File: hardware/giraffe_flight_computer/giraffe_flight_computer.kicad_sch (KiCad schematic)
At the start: 6 parts, among them J16 ADC, J2 PI, J4 ADC, J5 BAT, J6 BAT, J8 PI

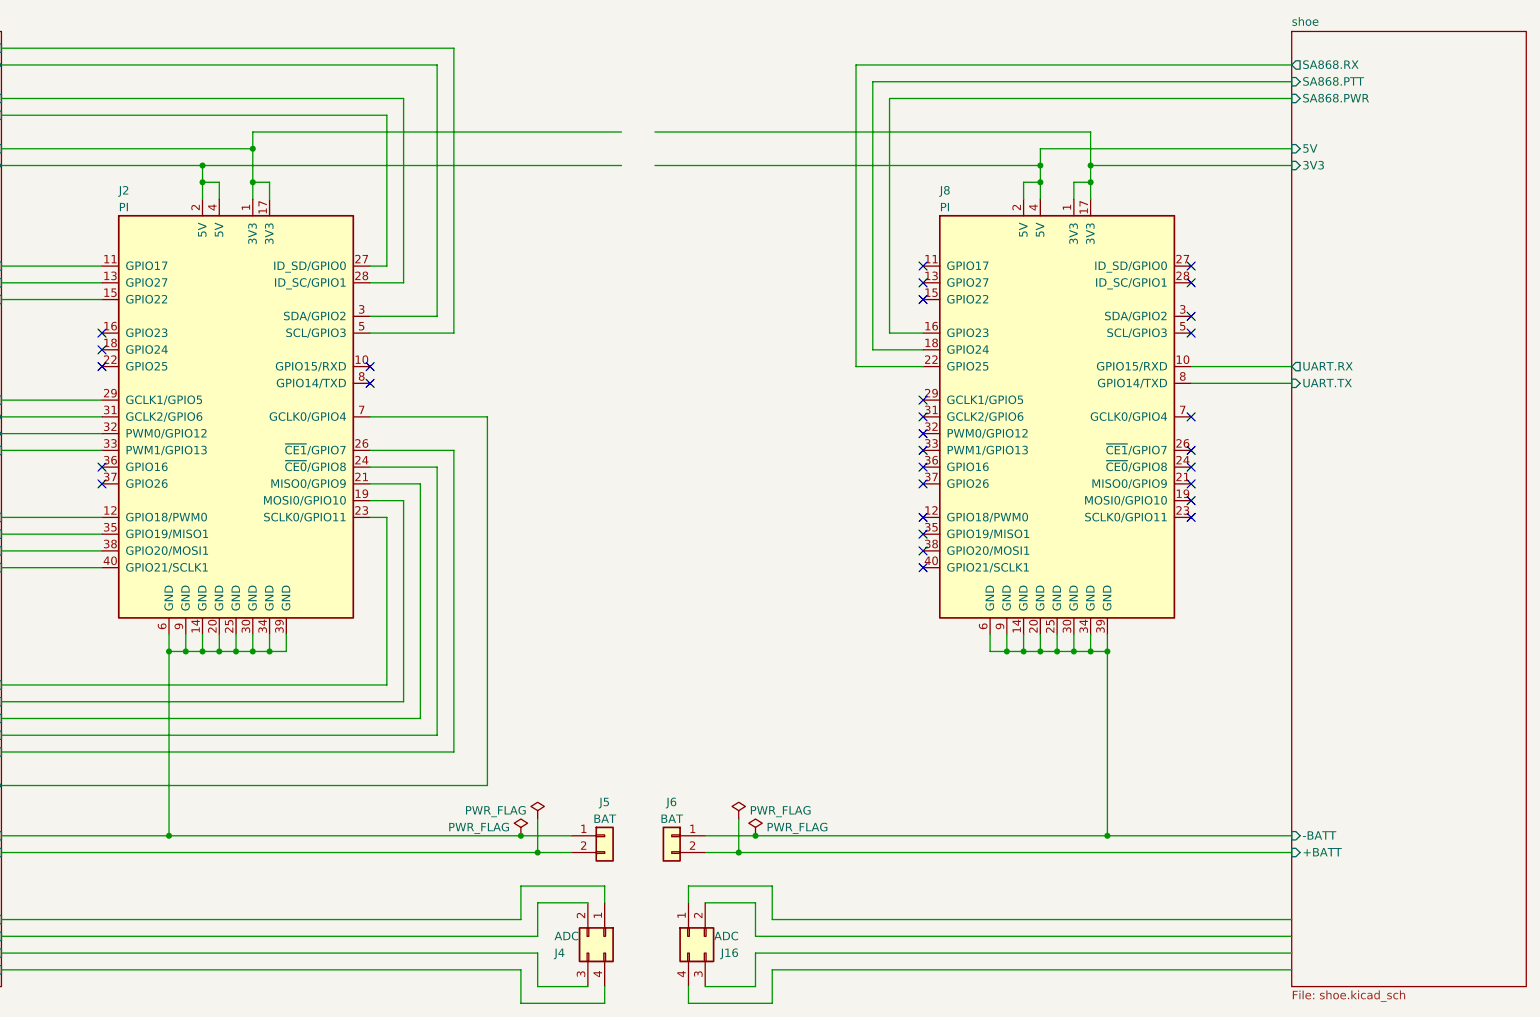
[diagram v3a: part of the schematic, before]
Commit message: More Schematic changes
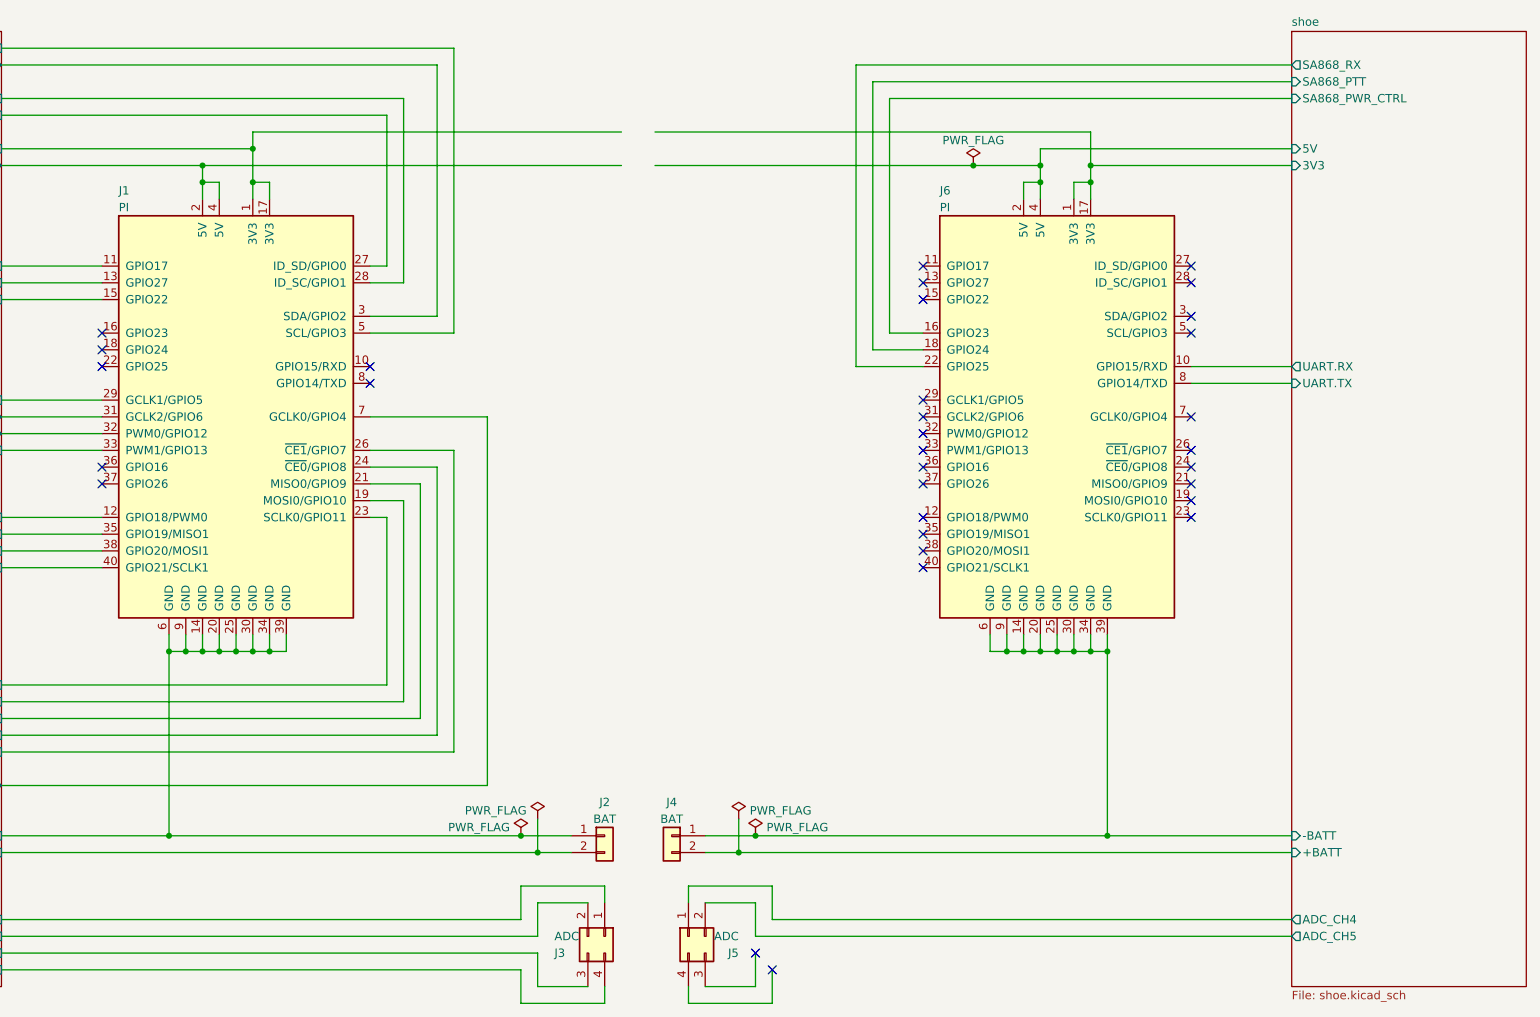
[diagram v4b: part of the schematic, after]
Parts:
- J2: renamed from J5; footprint (none) -> giraffe_flight_computer_footprints:battery_connection
- J4: renamed from J6; footprint (none) -> giraffe_flight_computer_footprints:battery_connection
- renumbered J2 to J1, J4 to J3, J16 to J5, J8 to J6
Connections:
- net shoe/ADC_CH4: now reaches J5.1 (Pin_1)
- net shoe/ADC_CH5: now reaches J5.2 (Pin_2)
- net shoe/SA868.PTT renamed shoe/SA868_PTT
- net shoe/SA868.PWR renamed shoe/SA868_PWR_CTRL
- net shoe/SA868.RX renamed shoe/SA868_RX
- no-connect marks 30 -> 32
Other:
- sheet shoe ports: added ADC_CH4, ADC_CH5, SA868_PTT, SA868_PWR_CTRL, SA868_RX; removed SA868.PTT, SA868.PWR, SA868.RX
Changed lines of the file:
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@@
   (junction (at 88.9 109.22) (diameter 0) (color 0 0 0 0)
+  )
+  (junction (at 198.12 35.56) (diameter 0) (color 0 0 0 0)
   )
   (junction (at 81.28 109.22) (diameter 0) (color 0 0 0 0)
@@
   (no_connect (at 231.14 78.74))
   (no_connect (at 231.14 58.42))
+  (no_connect (at 167.64 157.48))
   (no_connect (at 190.5 88.9))
   (no_connect (at 231.14 81.28))
@@
   (no_connect (at 231.14 53.34))
   (no_connect (at 190.5 93.98))
+  (no_connect (at 165.1 154.94))
   (no_connect (at 66.04 83.82))
   (no_connect (at 190.5 71.12))
@@
     (stroke (width 0) (type default))
   )
-  (wire (pts (xy 246.38 157.48) (xy 167.64 157.48))
-    (stroke (width 0) (type default))
-  )
   (wire (pts (xy 106.68 78.74) (xy 119.38 78.74))
     (stroke (width 0) (type default))
@@
     (stroke (width 0) (type default))
   )
-  (wire (pts (xy 246.38 154.94) (xy 165.1 154.94))
-    (stroke (width 0) (type default))
-  )
   (wire (pts (xy 162.56 139.7) (xy 246.38 139.7))
     (stroke (width 0) (type default))
@@
     (stroke (width 0) (type default))
   )
-  (wire (pts (xy 149.86 35.56) (xy 208.28 35.56))
+  (wire (pts (xy 149.86 35.56) (xy 198.12 35.56))
     (stroke (width 0) (type default))
   )
@@
   )
   (wire (pts (xy 157.48 137.16) (xy 165.1 137.16))
+    (stroke (width 0) (type default))
+  )
+  (wire (pts (xy 198.12 35.56) (xy 208.28 35.56))
     (stroke (width 0) (type default))
   )
@@
   (symbol (lib_id "giraffe_symbols:pi_zero") (at 210.82 73.66 0) (unit 1)
     (in_bom yes) (on_board yes) (dnp no)
-    (property "Reference" "J8" (at 193.04 39.37 0)
+    (property "Reference" "J6" (at 193.04 39.37 0)
       (effects (font (size 1.27 1.27)) (justify left))
     )
@@
       (project "giraffe_flight_computer"
         (path "/8b6d32d3-7736-4ef0-bfd7-9f676eec710d"
-          (reference "J8") (unit 1)
+          (reference "J6") (unit 1)
         )
       )
@@
   (symbol (lib_id "Connector_Generic:Conn_02x02_Counter_Clockwise") (at 142.24 152.4 270) (unit 1)
     (in_bom yes) (on_board yes) (dnp no)
-    (property "Reference" "J4" (at 134.62 154.94 90)
+    (property "Reference" "J3" (at 134.62 154.94 90)
       (effects (font (size 1.27 1.27)) (justify left))
     )
@@
       (project "giraffe_flight_computer"
         (path "/8b6d32d3-7736-4ef0-bfd7-9f676eec710d"
-          (reference "J4") (unit 1)
+          (reference "J3") (unit 1)
         )
       )
@@
   (symbol (lib_id "Connector_Generic:Conn_01x02") (at 152.4 137.16 0) (mirror y) (unit 1)
     (in_bom yes) (on_board yes) (dnp no)
-    (property "Reference" "J6" (at 152.4 132.08 0)
+    (property "Reference" "J4" (at 152.4 132.08 0)
       (effects (font (size 1.27 1.27)))
     )
@@
       (effects (font (size 1.27 1.27)))
     )
-    (property "Footprint" "" (at 152.4 137.16 0)
+    (property "Footprint" "giraffe_flight_computer_footprints:battery_connection" (at 152.4 137.16 0)
       (effects (font (size 1.27 1.27)) hide)
     )
@@
       (project "giraffe_flight_computer"
         (path "/8b6d32d3-7736-4ef0-bfd7-9f676eec710d"
-          (reference "J6") (unit 1)
+          (reference "J4") (unit 1)
+        )
+      )
+    )
+  )
+  (symbol (lib_id "power:PWR_FLAG") (at 198.12 35.56 0) (unit 1)
+    (in_bom yes) (on_board yes) (dnp no)
+    (property "Reference" "#FLG?" (at 198.12 33.655 0)
+      (effects (font (size 1.27 1.27)) hide)
+    )
+    (property "Value" "PWR_FLAG" (at 198.12 31.75 0)
+      (effects (font (size 1.27 1.27)))
+    )
+    (property "Footprint" "" (at 198.12 35.56 0)
+      (effects (font (size 1.27 1.27)) hide)
+    )
+    (property "Datasheet" "~" (at 198.12 35.56 0)
+      (effects (font (size 1.27 1.27)) hide)
+    )
+    (pin "1")
+    (instances
+      (project "giraffe_flight_computer"
+        (path "/8b6d32d3-7736-4ef0-bfd7-9f676eec710d/ba60804d-01a4-423f-89a4-e92a0bf73814"
+          (reference "#FLG?") (unit 1)
+        )
+        (path "/8b6d32d3-7736-4ef0-bfd7-9f676eec710d"
+          (reference "#FLG05") (unit 1)
         )
       )
@@
   (symbol (lib_id "Connector_Generic:Conn_02x02_Counter_Clockwise") (at 154.94 152.4 90) (mirror x) (unit 1)
     (in_bom yes) (on_board yes) (dnp no)
-    (property "Reference" "J16" (at 162.56 154.94 90)
+    (property "Reference" "J5" (at 162.56 154.94 90)
       (effects (font (size 1.27 1.27)) (justify left))
     )
@@
       (project "giraffe_flight_computer"
         (path "/8b6d32d3-7736-4ef0-bfd7-9f676eec710d"
-          (reference "J16") (unit 1)
+          (reference "J5") (unit 1)
         )
       )
@@
   (symbol (lib_id "giraffe_symbols:pi_zero") (at 86.36 73.66 0) (unit 1)
     (in_bom yes) (on_board yes) (dnp no)
-    (property "Reference" "J2" (at 68.58 39.37 0)
+    (property "Reference" "J1" (at 68.58 39.37 0)
       (effects (font (size 1.27 1.27)) (justify left))
     )
@@
       (project "giraffe_flight_computer"
         (path "/8b6d32d3-7736-4ef0-bfd7-9f676eec710d"
-          (reference "J2") (unit 1)
+          (reference "J1") (unit 1)
         )
       )
@@
   (symbol (lib_id "Connector_Generic:Conn_01x02") (at 142.24 137.16 0) (unit 1)
     (in_bom yes) (on_board yes) (dnp no)
-    (property "Reference" "J5" (at 142.24 132.08 0)
+    (property "Reference" "J2" (at 142.24 132.08 0)
       (effects (font (size 1.27 1.27)))
     )
@@
       (effects (font (size 1.27 1.27)))
     )
-    (property "Footprint" "" (at 142.24 137.16 0)
+    (property "Footprint" "giraffe_flight_computer_footprints:battery_connection" (at 142.24 137.16 0)
       (effects (font (size 1.27 1.27)) hide)
     )
@@
       (project "giraffe_flight_computer"
         (path "/8b6d32d3-7736-4ef0-bfd7-9f676eec710d"
-          (reference "J5") (unit 1)
+          (reference "J2") (unit 1)
         )
       )
@@
       (effects (font (size 1.27 1.27)) (justify left))
     )
-    (pin "SA868.PWR" input (at 246.38 25.4 180)
-      (effects (font (size 1.27 1.27)) (justify left))
-    )
-    (pin "SA868.RX" output (at 246.38 20.32 180)
-      (effects (font (size 1.27 1.27)) (justify left))
-    )
-    (pin "SA868.PTT" input (at 246.38 22.86 180)
-      (effects (font (size 1.27 1.27)) (justify left))
-    )
+    (pin "SA868_PWR_CTRL" input (at 246.38 25.4 180)
+      (effects (font (size 1.27 1.27)) (justify left))
+    )
+    (pin "SA868_RX" output (at 246.38 20.32 180)
+      (effects (font (size 1.27 1.27)) (justify left))
+    )
+    (pin "SA868_PTT" input (at 246.38 22.86 180)
+      (effects (font (size 1.27 1.27)) (justify left))
+    )
+    (pin "ADC_CH5" output (at 246.38 152.4 180)
+      (effects (font (size 1.27 1.27)) (justify left))
+    )
+    (pin "ADC_CH4" output (at 246.38 149.86 180)
+      (effects (font (size 1.27 1.27)) (justify left))
+    )

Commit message: Rev A Hat Complete
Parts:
- removed J5: ADC, Connector_PinSocket_1.27mm:PinSocket_2x02_P1.27mm_Vertical, symbol Connector_Generic:Conn_02x02_Counter_Clockwise
- added J5: ADC, Connector_PinHeader_1.27mm:PinHeader_1x01_P1.27mm_Vertical, symbol Connector_Generic:Conn_01x01
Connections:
- net hat/BMI088.INT1: now also J1.31 (GCLK2/GPIO6); no longer J1.29 (GCLK1/GPIO5)
- net hat/BMI088.INT3: now also J1.29 (GCLK1/GPIO5); no longer J1.31 (GCLK2/GPIO6)
- net hat/SAM_M8Q.RST: now also J1.32 (PWM0/GPIO12); no longer J1.33 (PWM1/GPIO13)
- net hat/SAM_M8Q.TX_RDY: now also J1.33 (PWM1/GPIO13); no longer J1.32 (PWM0/GPIO12)
- net hat/STATUS_LED.BLUE: now also J1.11 (GPIO17); no longer J1.15 (GPIO22)
- net hat/STATUS_LED.RED: now also J1.15 (GPIO22); no longer J1.11 (GPIO17)
- net shoe/ADC_CH4: now also J5.1 (Pin_1)
- net hat/-BATT renamed hat/H_GND
- net hat/3V3 renamed hat/H_3V3
- net hat/5V renamed hat/H_5V
- net shoe/-BATT renamed shoe/S_GND
- net shoe/3V3 renamed shoe/S_3V3
- net shoe/5V renamed shoe/S_5V
- no-connect marks 32 -> 30
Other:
- sheet hat ports: added H_3V3, H_5V, H_GND; removed -BATT, 3V3, 5V
- sheet shoe ports: added S_3V3, S_5V, S_GND; removed -BATT, 3V3, 5V, ADC_CH5
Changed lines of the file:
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@@
   (no_connect (at 231.14 78.74))
   (no_connect (at 231.14 58.42))
-  (no_connect (at 167.64 157.48))
   (no_connect (at 190.5 88.9))
   (no_connect (at 231.14 81.28))
@@
   (no_connect (at 231.14 53.34))
   (no_connect (at 190.5 93.98))
-  (no_connect (at 165.1 154.94))
   (no_connect (at 66.04 83.82))
   (no_connect (at 190.5 71.12))
@@
     (stroke (width 0) (type default))
   )
-  (wire (pts (xy 167.64 157.48) (xy 167.64 162.56))
-    (stroke (width 0) (type default))
-  )
-  (wire (pts (xy 246.38 149.86) (xy 167.64 149.86))
+  (wire (pts (xy 157.48 152.4) (xy 246.38 152.4))
     (stroke (width 0) (type default))
   )
@@
     (stroke (width 0) (type default))
   )
-  (wire (pts (xy 167.64 162.56) (xy 154.94 162.56))
-    (stroke (width 0) (type default))
-  )
   (wire (pts (xy 106.68 88.9) (xy 109.22 88.9))
     (stroke (width 0) (type default))
@@
     (stroke (width 0) (type default))
   )
-  (wire (pts (xy 246.38 152.4) (xy 165.1 152.4))
-    (stroke (width 0) (type default))
-  )
-  (wire (pts (xy 165.1 160.02) (xy 157.48 160.02))
-    (stroke (width 0) (type default))
-  )
-  (wire (pts (xy 165.1 147.32) (xy 157.48 147.32))
-    (stroke (width 0) (type default))
-  )
   (wire (pts (xy 76.2 106.68) (xy 76.2 109.22))
     (stroke (width 0) (type default))
@@
     (stroke (width 0) (type default))
   )
-  (wire (pts (xy 165.1 147.32) (xy 165.1 152.4))
-    (stroke (width 0) (type default))
-  )
-  (wire (pts (xy 167.64 149.86) (xy 167.64 144.78))
-    (stroke (width 0) (type default))
-  )
   (wire (pts (xy 106.68 53.34) (xy 111.76 53.34))
     (stroke (width 0) (type default))
@@
     (stroke (width 0) (type default))
   )
-  (wire (pts (xy 165.1 154.94) (xy 165.1 160.02))
-    (stroke (width 0) (type default))
-  )
   (wire (pts (xy 231.14 68.58) (xy 246.38 68.58))
     (stroke (width 0) (type default))
@@
     (stroke (width 0) (type default))
   )
-  (wire (pts (xy 167.64 144.78) (xy 154.94 144.78))
-    (stroke (width 0) (type default))
-  )
   (wire (pts (xy 218.44 106.68) (xy 218.44 109.22))
     (stroke (width 0) (type default))
@@
     (stroke (width 0) (type default))
   )
-  (wire (pts (xy 154.94 162.56) (xy 154.94 160.02))
-    (stroke (width 0) (type default))
-  )
   (wire (pts (xy 91.44 40.64) (xy 91.44 38.1))
     (stroke (width 0) (type default))
@@
   )
   (wire (pts (xy 83.82 38.1) (xy 81.28 38.1))
-    (stroke (width 0) (type default))
-  )
-  (wire (pts (xy 154.94 147.32) (xy 154.94 144.78))
     (stroke (width 0) (type default))
   )
@@
     )
   )
+  (symbol (lib_id "Connector_Generic:Conn_01x01") (at 152.4 152.4 180) (unit 1)
+    (in_bom yes) (on_board yes) (dnp no)
+    (property "Reference" "J5" (at 152.4 147.32 0)
+      (effects (font (size 1.27 1.27)))
+    )
+    (property "Value" "ADC" (at 152.4 149.86 0)
+      (effects (font (size 1.27 1.27)))
+    )
+    (property "Footprint" "Connector_PinHeader_1.27mm:PinHeader_1x01_P1.27mm_Vertical" (at 152.4 152.4 0)
+      (effects (font (size 1.27 1.27)) hide)
+    )
+    (property "Datasheet" "~" (at 152.4 152.4 0)
+      (effects (font (size 1.27 1.27)) hide)
+    )
+    (pin "1")
+    (instances
+      (project "giraffe_flight_computer"
+        (path "/8b6d32d3-7736-4ef0-bfd7-9f676eec710d"
+          (reference "J5") (unit 1)
+        )
+      )
+    )
+  )
   (symbol (lib_id "power:PWR_FLAG") (at 165.1 137.16 0) (unit 1)
     (in_bom yes) (on_board yes) (dnp no)
@@
         (path "/8b6d32d3-7736-4ef0-bfd7-9f676eec710d"
           (reference "#FLG04") (unit 1)
-        )
-      )
-    )
-  )
-  (symbol (lib_id "Connector_Generic:Conn_02x02_Counter_Clockwise") (at 154.94 152.4 90) (mirror x) (unit 1)
-    (in_bom yes) (on_board yes) (dnp no)
-    (property "Reference" "J5" (at 162.56 154.94 90)
-      (effects (font (size 1.27 1.27)) (justify left))
-    )
-    (property "Value" "ADC" (at 162.56 152.4 90)
-      (effects (font (size 1.27 1.27)) (justify left))
-    )
-    (property "Footprint" "Connector_PinSocket_1.27mm:PinSocket_2x02_P1.27mm_Vertical" (at 154.94 152.4 0)
-      (effects (font (size 1.27 1.27)) hide)
-    )
-    (property "Datasheet" "~" (at 154.94 152.4 0)
-      (effects (font (size 1.27 1.27)) hide)
-    )
-    (pin "1")
-    (pin "2")
-    (pin "3")
-    (pin "4")
-    (instances
-      (project "giraffe_flight_computer"
-        (path "/8b6d32d3-7736-4ef0-bfd7-9f676eec710d"
-          (reference "J5") (unit 1)
         )
       )
@@
       (effects (font (size 1.27 1.27)) (justify right))
     )
-    (pin "3V3" input (at 50.8 33.02 0)
-      (effects (font (size 1.27 1.27)) (justify right))
-    )
-    (pin "5V" output (at 50.8 35.56 0)
+    (pin "H_3V3" input (at 50.8 33.02 0)
+      (effects (font (size 1.27 1.27)) (justify right))
+    )
+    (pin "H_5V" output (at 50.8 35.56 0)
       (effects (font (size 1.27 1.27)) (justify right))
     )
@@
       (effects (font (size 1.27 1.27)) (justify right))
     )
-    (pin "-BATT" input (at 50.8 137.16 0)
-      (effects (font (size 1.27 1.27)) (justify right))
-    )
-    (pin "BMI088.INT3" output (at 50.8 73.66 0)
-      (effects (font (size 1.27 1.27)) (justify right))
-    )
-    (pin "BMI088.INT1" input (at 50.8 71.12 0)
-      (effects (font (size 1.27 1.27)) (justify right))
-    )
-    (pin "SAM_M8Q.RST" input (at 50.8 78.74 0)
-      (effects (font (size 1.27 1.27)) (justify right))
-    )
-    (pin "SAM_M8Q.TX_RDY" output (at 50.8 76.2 0)
-      (effects (font (size 1.27 1.27)) (justify right))
-    )
-    (pin "STATUS_LED.RED" input (at 50.8 50.8 0)
+    (pin "H_GND" input (at 50.8 137.16 0)
       (effects (font (size 1.27 1.27)) (justify right))
     )
@@
       (effects (font (size 1.27 1.27)) (justify right))
     )
-    (pin "STATUS_LED.BLUE" input (at 50.8 55.88 0)
-      (effects (font (size 1.27 1.27)) (justify right))
-    )
     (pin "PCM.DIN" input (at 50.8 93.98 0)
       (effects (font (size 1.27 1.27)) (justify right))
@@
     )
     (pin "ADC.CH7" input (at 50.8 157.48 0)
+      (effects (font (size 1.27 1.27)) (justify right))
+    )
+    (pin "SAM_M8Q.TX_RDY" output (at 50.8 78.74 0)
+      (effects (font (size 1.27 1.27)) (justify right))
+    )
+    (pin "SAM_M8Q.RST" input (at 50.8 76.2 0)
+      (effects (font (size 1.27 1.27)) (justify right))
+    )
+    (pin "STATUS_LED.RED" input (at 50.8 55.88 0)
+      (effects (font (size 1.27 1.27)) (justify right))
+    )
+    (pin "STATUS_LED.BLUE" input (at 50.8 50.8 0)
+      (effects (font (size 1.27 1.27)) (justify right))
+    )
+    (pin "BMI088.INT3" input (at 50.8 71.12 0)
+      (effects (font (size 1.27 1.27)) (justify right))
+    )
+    (pin "BMI088.INT1" input (at 50.8 73.66 0)
       (effects (font (size 1.27 1.27)) (justify right))
     )
@@
       (effects (font (size 1.27 1.27)) (justify left top))
     )
-    (pin "3V3" input (at 246.38 35.56 180)
+    (pin "S_3V3" input (at 246.38 35.56 180)
       (effects (font (size 1.27 1.27)) (justify left))
     )
@@
       (effects (font (size 1.27 1.27)) (justify left))
     )
-    (pin "-BATT" input (at 246.38 137.16 180)
-      (effects (font (size 1.27 1.27)) (justify left))
-    )
-    (pin "5V" input (at 246.38 33.02 180)
+    (pin "S_GND" input (at 246.38 137.16 180)
+      (effects (font (size 1.27 1.27)) (justify left))
+    )
+    (pin "S_5V" input (at 246.38 33.02 180)
       (effects (font (size 1.27 1.27)) (justify left))
     )
@@
       (effects (font (size 1.27 1.27)) (justify left))
     )
-    (pin "ADC_CH5" output (at 246.38 152.4 180)
-      (effects (font (size 1.27 1.27)) (justify left))
-    )
-    (pin "ADC_CH4" output (at 246.38 149.86 180)
-      (effects (font (size 1.27 1.27)) (justify left))
-    )
+    (pin "ADC_CH4" output (at 246.38 152.4 180)
+      (effects (font (size 1.27 1.27)) (justify left))
+    )
